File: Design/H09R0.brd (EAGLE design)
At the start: 34.6 x 30 mm, 32 parts, among them P2 HEXABIT_17.32_NO_P6, P3 691311500102, U2 AD8495ARMZ-R7, U3 TLVH431ACDBVR, X1 XTALL_CSTCE8M00G52

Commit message: - Deleted old output files - Changed MCU to G0 - New schematic - New layout - Generated documentation - Generated BOM
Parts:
- removed B, C, D: PAD1, Hexabitz:PAD1
- removed C3, C4: 4.7uF, Hexabitz:C-0805-POL
- removed C5: 10nF, Hexabitz:C-0603
- removed C6: 100nF, Hexabitz:C-0603
- removed U1: (no value), Hexabitz:STM32F091CBU6
- added D2: ORANGE, HEXABITZ_USER_INTERFACE_PARTS:VLMS1300-GS08
- added D3: YELLOW, HEXABITZ_USER_INTERFACE_PARTS:VLMS1300-GS08
- added D5: BOURNS_CDSOD323-T03SCBOURNS_CDSOD323-T03SC_0_0, HEXABITZ_RCLS:BOURNS_CDSOD323-T03SC_0
- added R11: 1M, Hexabitz:R-0402
- added R9: 270.0R, HEXABITZ_RCLS:R-0603
- added SWD1: (no value), pinhead:1X03
- added U4: STM32G0B1CEU6QFN_B1CEU6_STM-L, HEXABITZ_ICs:QFN_B1CEU6_STM-L
- C1: value 100nF -> 1uF; device Hexabitz:C-0603 -> HEXABITZ_RCLS:C-0805
- C2: value 1.00uF -> 100nF; device Hexabitz:C-0805-POL -> HEXABITZ_RCLS:C-0603
- C7, C8: device Hexabitz:C-0603 -> HEXABITZ_RCLS:C-0603
- C9: value 100nF -> 4.7uF; device Hexabitz:C-0603 -> HEXABITZ_RCLS:C-0805
- D1: value VLMS1300-GS08 -> RED; device Hexabitz:VLMS1300-GS08 -> HEXABITZ_USER_INTERFACE_PARTS:VLMS1300-GS08
- FB1: device Hexabitz:FB-TDK_MMZ1608Y300B -> HEXABITZ_RCLS:FB-0603
- P2: device Hexabitz:HEXABIT_17.32_NO_P6 -> hexabitz_connectors:HEXABIT_17.32_NO_P6
- R: value PAD1 -> R; device Hexabitz:PAD1 -> HEXABITZ_USER_INTERFACE_PARTS:1X01
- R1: value 270.0R -> 0.0R; device Hexabitz:R-0603 -> HEXABITZ_RCLS:R-0603
- R2: value 10.0K -> 270R; device Hexabitz:R-0603 -> HEXABITZ_RCLS:R-0603
- R3: value 0.0R -> 10K; device Hexabitz:R-0603 -> HEXABITZ_RCLS:R-0603
- R8: value 1M -> 270.0R; device Hexabitz:R-0402 -> HEXABITZ_RCLS:R-0603
- X1: device Hexabitz:XTALL_CSTCE8M00G52 -> HEXABITZ_RCLS:XTALL_CSTCE8M00G52
- moved R1 19.3 mm to (26.5, 13.2), flipped to the bottom, turned to 90 degrees
- moved R2 18.2 mm to (17.8, 7.70), turned to 270 degrees
- moved R3 16.3 mm to (11.4, 17.0)
- moved R 14.3 mm to (23.0, 4.68)
- moved C7 13.6 mm to (23.4, 17.1), turned to 180 degrees
- moved D1 13.4 mm to (16.7, 6.17), turned to 270 degrees
- moved FB1 8.73 mm to (23.4, 20.1), flipped to the bottom, turned to 180 degrees
- moved R8 7.95 mm to (18.8, 19.4), flipped to the bottom, turned to 270 degrees
- moved C2 5.92 mm to (23.2, 7.44), turned to 180 degrees
- moved X1 5.02 mm to (23.1, 11.1), turned to 180 degrees
- moved C9 4.95 mm to (23.4, 14.6)
- moved C8 3.88 mm to (23.4, 18.0), turned to 180 degrees
- moved R4 3.37 mm to (13.0, 4.80), turned to 0 degrees
- moved C1 3.07 mm to (23.4, 16.0), turned to 180 degrees
- moved P2 0.11 mm to (17.2, 14.9)
- renumbered P3 to JP1
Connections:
- removed net B: B.P$1, B.P$2, R2.2, U1.P$44
- removed net N$1: D.P$1, D.P$2, U1.P$34
- removed net N$2: C.P$1, C.P$2, U1.P$37
- removed net R: C1.1, R.P$1, R.P$2, U1.P$7
- removed net USART1_RX: P2.23, U1.P$31
- removed net USART1_TX: P2.17, U1.P$30
- new net CLK: R3.2, SWD1.1, SWD1.2, U4.36
- new net DATA: SWD1.3, U4.35
- new net N$16: D1.A, R2.2
- new net N$17: R8.2, U4.44
- new net N$18: R9.2, U4.43
- new net N$19: D2.A, R9.1
- new net N$20: D3.A, R8.1
- new net USART5_RX: P2.PAD_PD4, U4.20
- new net USART5_TX: P2.PAD_PU4, U4.19
- net GND: now also C2.2, D2.C, D3.C, D5.1, P2.PAD_PD10, P2.PAD_PD11, P2.PAD_PD12, P2.PAD_PD7, P2.PAD_PD8, P2.PAD_PD9, R1.1, R11.1, U4.49; no longer C1.2, C3.2, C4.2, C6.2, C7.2, C8.2, C9.2, P2.10, P2.11, P2.12, P2.7, P2.8, P2.9, R2.1, R8.1, U1.EP, U1.P$23, U1.P$35, U1.P$47
- net N$10: now also U4.8, X1.P$3; no longer D1.A, R1.1
- net N$14: now also C2.1, R.1, U4.10; no longer U1.P$5, X1.P$1
- net N$15: now also R2.1, U4.17; no longer U1.P$6, X1.P$3
- net N$8: now also U4.9, X1.P$1; no longer R1.2, U1.P$32
- net TEMP1: no longer U1.P$17
- net TYPE_K_THC_IN-: now also R11.2; no longer R8.2
- net USART2_RX: now also P2.PAD_PD3, U4.14; no longer P2.20, U1.P$13
- net USART2_TX: now also P2.PAD_PU3, U4.13; no longer P2.14, U1.P$12
- net USART3_RX: now also P2.PAD_PD5, U4.23; no longer P2.22, U1.P$22
- net USART3_TX: now also P2.PAD_PU5, U4.22; no longer P2.16, U1.P$21
- net USART4_RX: now also P2.PAD_PD2, U4.12; no longer P2.19, U1.P$11
- net USART4_TX: now also P2.PAD_PU2, U4.11; no longer P2.13, U1.P$10
- net USART6_RX: now also P2.PAD_PD1, U4.48; no longer P2.21, U1.P$15
- net USART6_TX: now also P2.PAD_PU1, U4.47; no longer P2.15, U1.P$14
- net VDD: now also D5.2, P2.PAD_PU10, P2.PAD_PU11, P2.PAD_PU12, P2.PAD_PU7, P2.PAD_PU8, P2.PAD_PU9; no longer C3.1, C4.1, C6.1, C7.1, C8.1, C9.1, P2.1, P2.2, P2.3, P2.4, P2.5, P2.6, U1.P$1, U1.P$24, U1.P$36, U1.P$48
- net VDDA: now also C1.1, C7.1, C8.1, C9.1, U4.4, U4.5, U4.6; no longer C2.1, C5.1, U1.P$9
- net VSSA: now also C1.2, C7.2, C8.2, C9.2, R1.2, U4.7; no longer C2.2, C5.2, R3.2, U1.P$8
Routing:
- net GND: track 150.9 -> 40.3 mm, vias 19 -> 8
- net VDD: track 45.4 -> 8.40 mm, vias 3 -> 1
- net USART5_TX: track 0.00 -> 17.4 mm, vias 0 -> 1
- net USART1_TX: track 16.2 -> 0.00 mm, vias 1 -> 0
- net B: track 15.6 -> 0.00 mm, vias 1 -> 0
- net USART5_RX: track 0.00 -> 15.5 mm
- net N$2: track 15.2 -> 0.00 mm, vias 2 -> 0
- net USART1_RX: track 14.7 -> 0.00 mm
- net R: track 13.7 -> 0.00 mm, vias 2 -> 0
- net DATA: track 0.00 -> 8.81 mm
- net N$1: track 8.41 -> 0.00 mm, vias 1 -> 0
- net USART3_RX: track 13.5 -> 21.7 mm
- net CLK: track 0.00 -> 7.69 mm
- net USART3_TX: track 15.6 -> 22.3 mm
- net USART4_RX: track 24.0 -> 18.8 mm
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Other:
- board text added: "H09R01"
- board text removed: "H09R00"
- board text removed: "R"
- board text removed: "Total Thickness 1.6 mm --------------------------------------------------------- copper_top.gbr : Top Conductor - Copper: Thickness 0.035 mm Dielectric - FR-4: copper_bottom.gbr : Bottom Conductor - Copper: Thickness 0.035 mm"

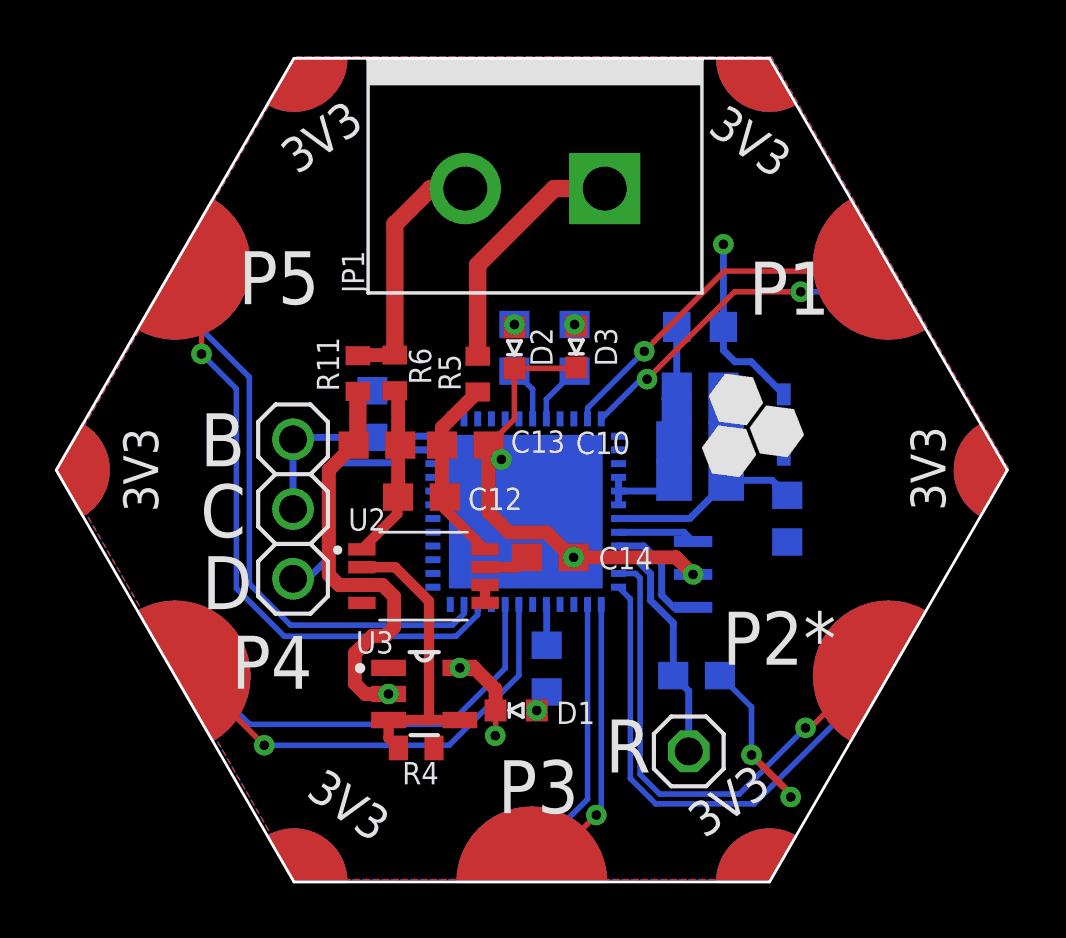
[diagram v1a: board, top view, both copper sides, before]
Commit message: - Deleted yellow and orange LEDs from design - Changed connector - Changed RESs and CAPs and used from our library - New layout - Changed polygon to thermal - Rearranged compenents in BOM
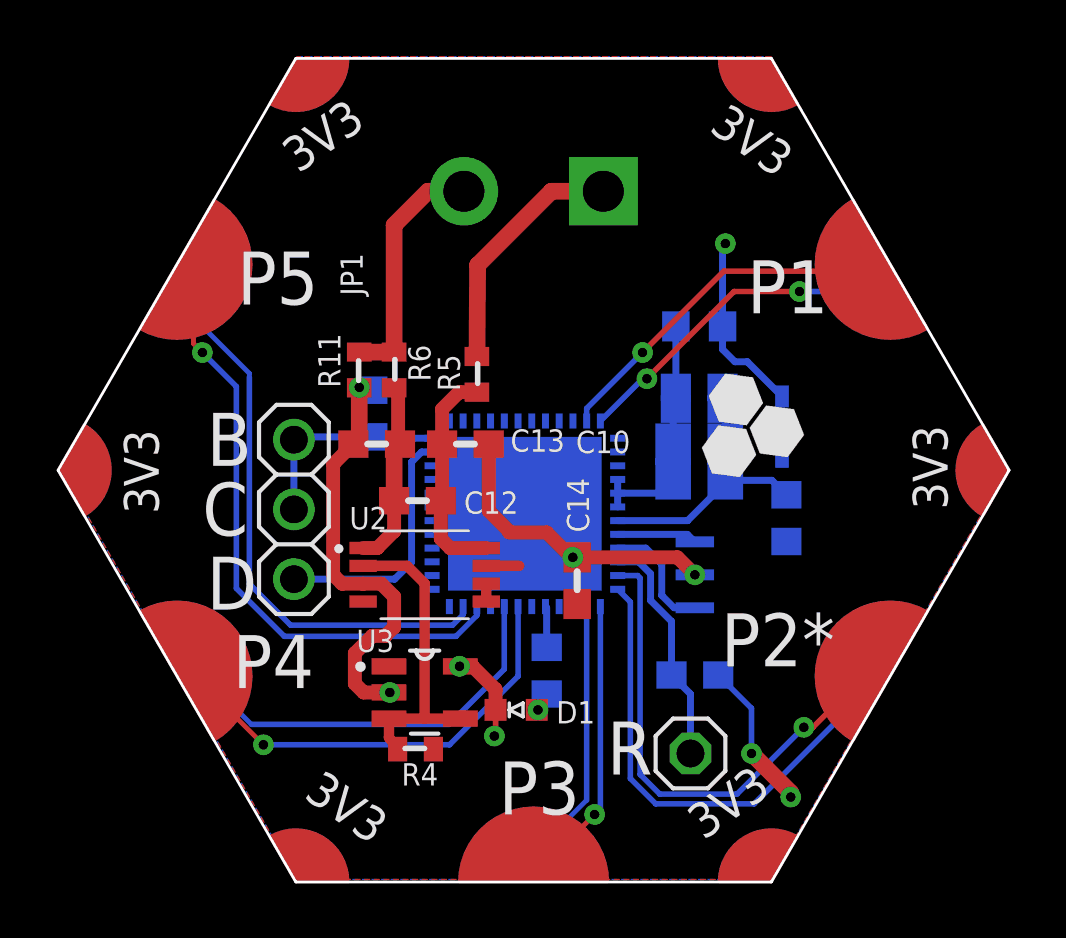
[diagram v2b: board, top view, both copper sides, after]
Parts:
- removed D2: ORANGE, HEXABITZ_USER_INTERFACE_PARTS:VLMS1300-GS08
- removed D3: YELLOW, HEXABITZ_USER_INTERFACE_PARTS:VLMS1300-GS08
- removed R8, R9: 270.0R, HEXABITZ_RCLS:R-0603
- C10, C12, C13, C14: device Hexabitz:C-0603 -> HEXABITZ_RCLS:C-0603
- JP1: device Hexabitz:691311500102 -> HEXABITZ_CONNECTION_PARTS:1546111-2
- R11, R4, R5, R6: device Hexabitz:R-0402 -> HEXABITZ_RCLS:R-0402
- moved C14 1.30 mm to (18.9, 10.9), turned to 90 degrees
- moved C12 0.20 mm to (13.1, 13.8)
- moved R11 0.14 mm to (11.0, 18.6)
- moved R6 0.11 mm to (12.2, 18.6)
- moved JP1 0.11 mm to (17.3, 25.1)
- moved D5 0.10 mm to (26.4, 16.5)
- moved R 0.10 mm to (23.0, 4.60)
- moved C1 0.08 mm to (23.3, 15.9)
- moved U4 0.08 mm to (17.0, 13.3)
- moved R2 0.08 mm to (17.8, 7.62)
- moved P2 0.07 mm to (17.3, 14.9)
- moved C2 0.07 mm to (23.2, 7.46)
- moved U2 0.07 mm to (13.3, 11.1)
- moved X1 0.06 mm to (23.2, 11.1)
- moved C9 0.06 mm to (23.3, 14.6)
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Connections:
- removed net N$17: R8.2, U4.44
- removed net N$18: R9.2, U4.43
- removed net N$19: D2.A, R9.1
- removed net N$20: D3.A, R8.1
- net GND: no longer D2.C, D3.C
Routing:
- net GND: track 40.3 -> 37.4 mm
- net N$17: track 2.16 -> 0.00 mm
- net N$18: track 2.01 -> 0.00 mm
- net N$3: track 6.92 -> 8.07 mm
- net USART2_RX: track 11.2 -> 10.3 mm
- net USART3_RX: track 21.7 -> 21.0 mm
- net USART5_TX: track 17.4 -> 16.8 mm
- net N$20: track 0.57 -> 0.00 mm, vias 1 -> 0
- net N$7: track 6.49 -> 7.02 mm
- net N$19: track 0.10 -> 0.00 mm, vias 1 -> 0
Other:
- board text added: "IN+"
- board text added: "IN-"

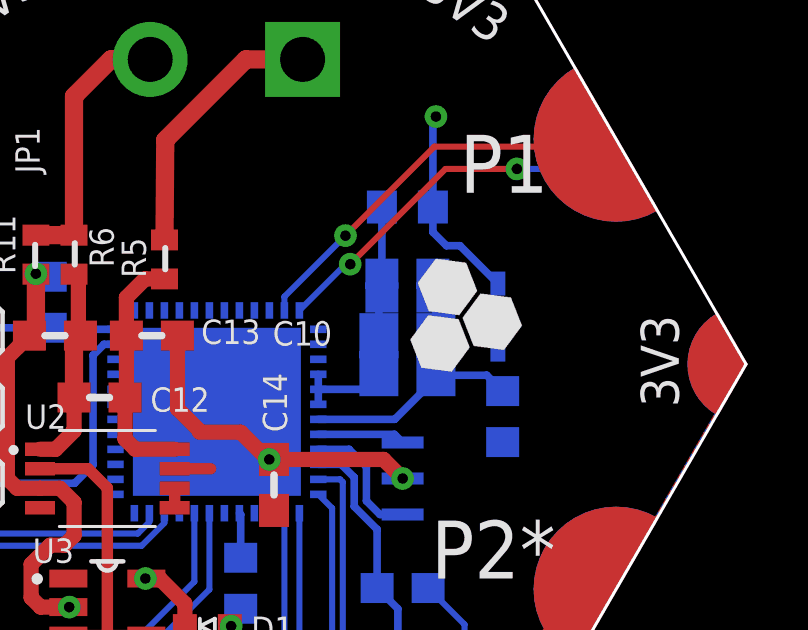
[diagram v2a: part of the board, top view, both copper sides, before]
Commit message: - Changed logo in layout - Rearranged components in BOM
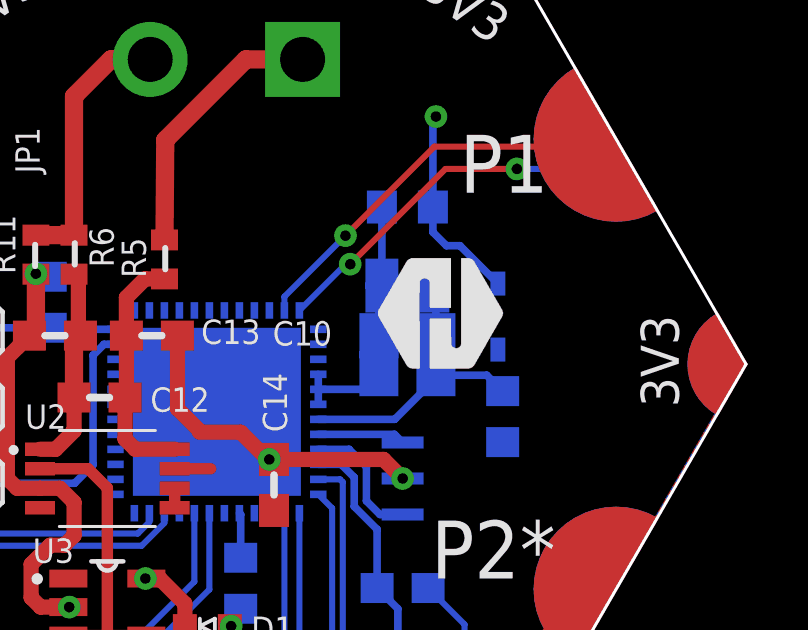
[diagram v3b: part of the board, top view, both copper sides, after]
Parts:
- added U$1: (no value), HEXABITZ_USER_INTERFACE_PARTS:HEXA-LOGO
